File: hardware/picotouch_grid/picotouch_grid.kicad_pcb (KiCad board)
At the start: 2 copper layers, 180 x 110 mm, 125 parts, among them U1 Pico, U2 TS20, U3 TS20

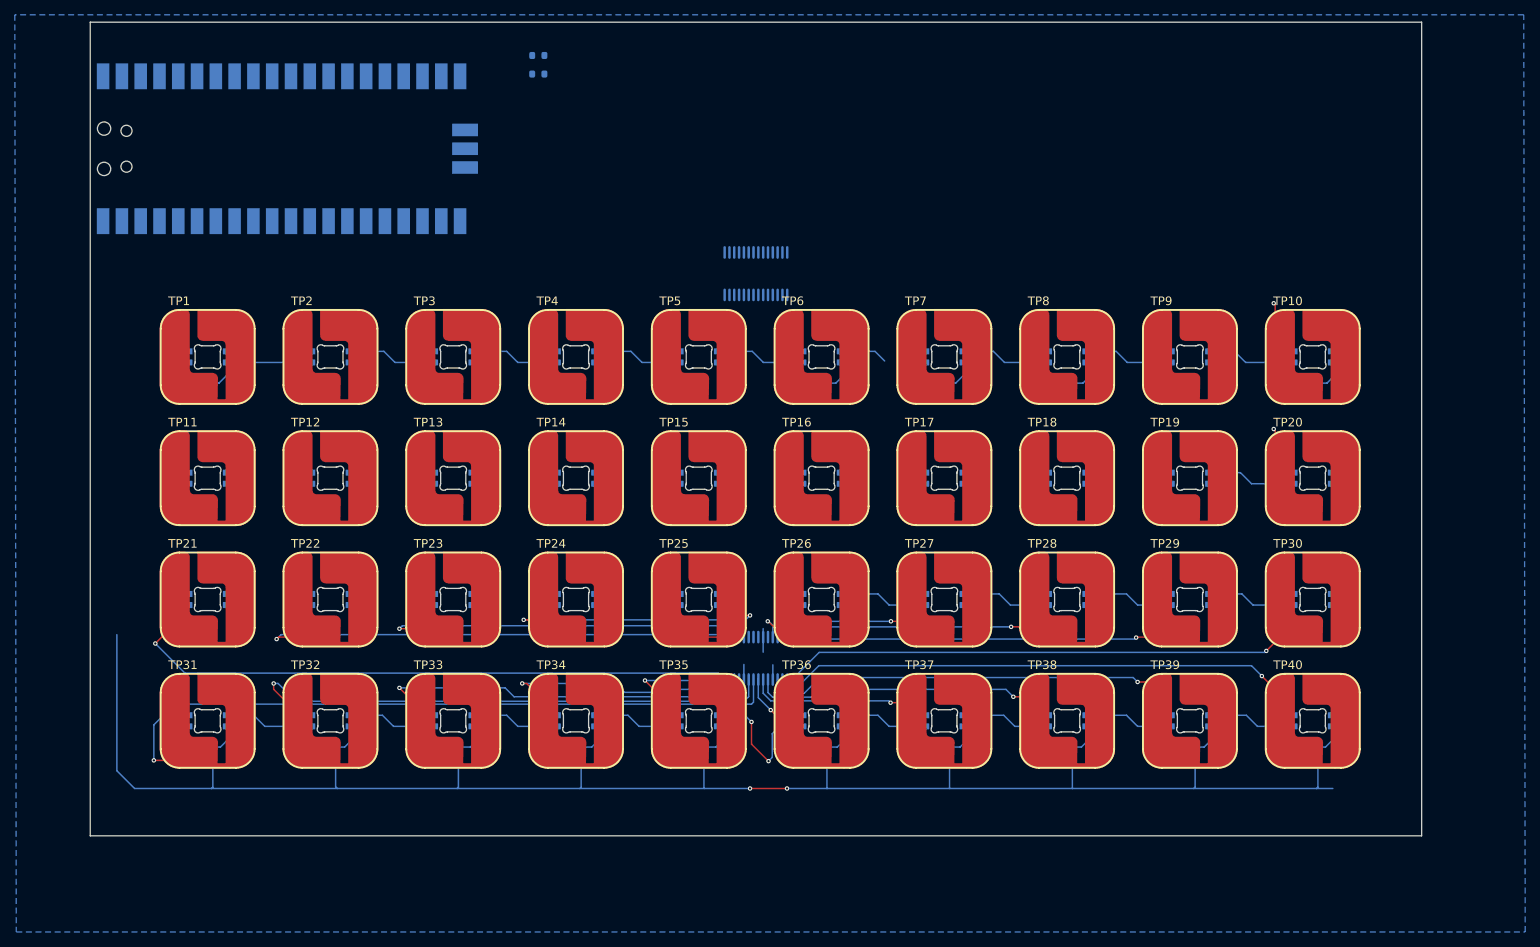
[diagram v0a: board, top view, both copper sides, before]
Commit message: more pcb routing done
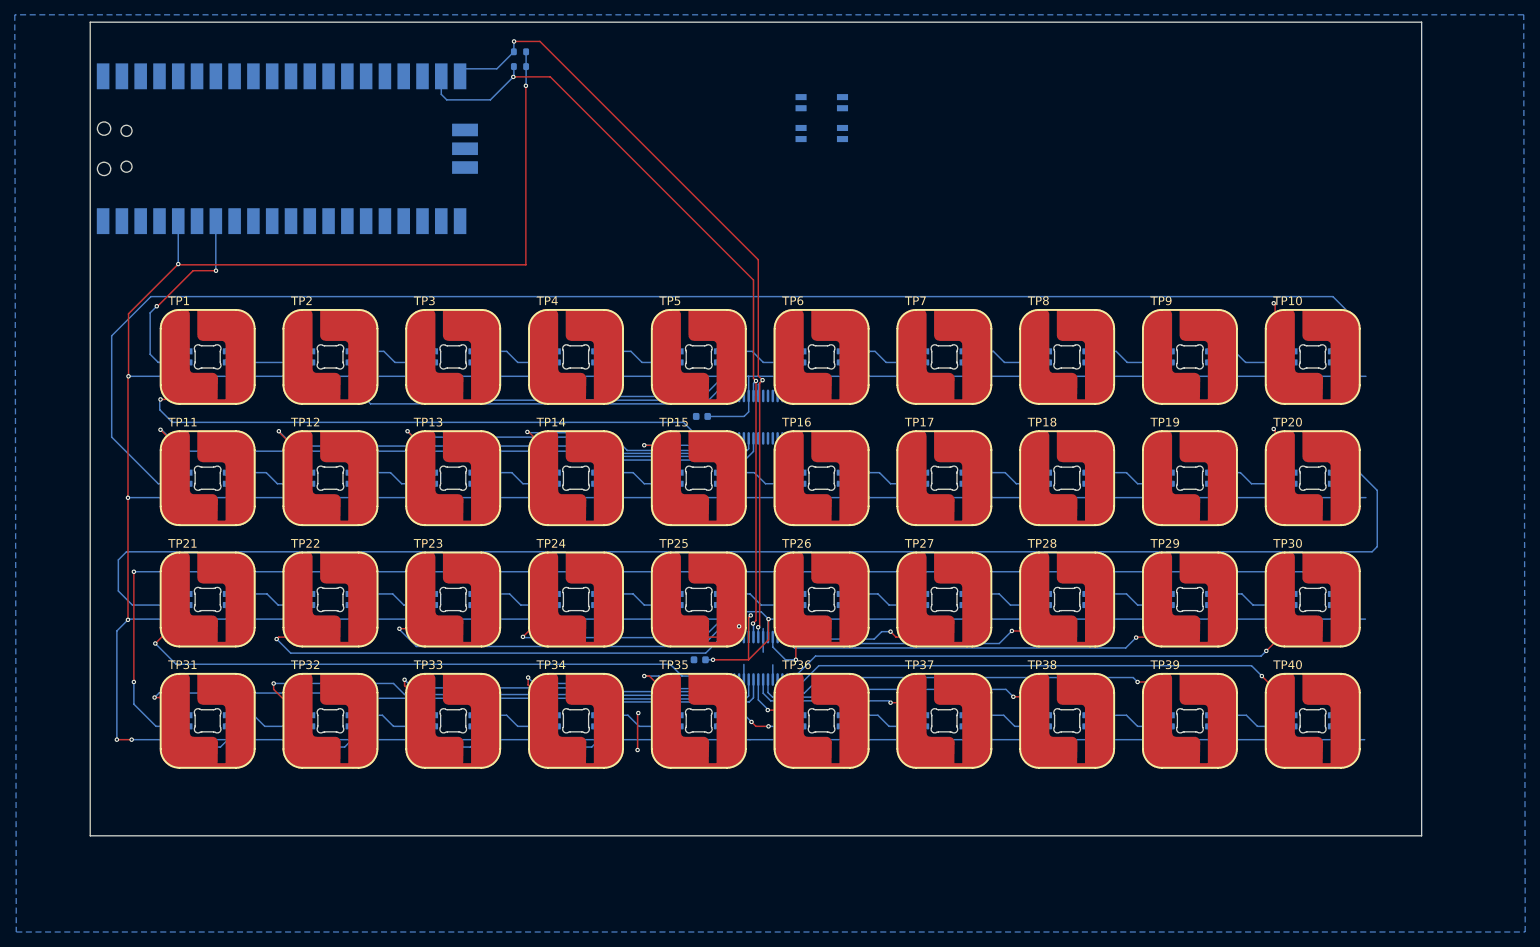
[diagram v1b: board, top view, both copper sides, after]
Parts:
- added C41: 1uF, Capacitor_SMD:C_0603_1608Metric, B.Cu at (119.7, 78.3)
- added C42: 1uF, Capacitor_SMD:C_0603_1608Metric, B.Cu at (119.4, 111.2)
- added U4: SK6812MINI-E_C5149201, easyeda2kicad:LED-SMD_L3.2-W2.8-TR, B.Cu at (135.9, 35.9)
- added U5: SK6812MINI-E_C5149201, easyeda2kicad:LED-SMD_L3.2-W2.8-TR, B.Cu at (135.9, 40.0)
- moved U2 19.4 mm to (127.0, 78.4)
- moved R2 3.90 mm to (95.1, 29.0)
- moved R1 2.89 mm to (95.1, 31.0)
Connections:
- LED1 pad 3: unconnected-(LED1-DIN-Pad3) -> /NEOPIXEL_DATA
- U1 pad 34: unconnected-(U1-GPIO28_ADC2-Pad34) -> /NEOPIXEL_DATA
- U2 pad 11: unconnected-(U2-CS13-Pad11) -> /tp13
- U2 pad 12: unconnected-(U2-CS14-Pad12) -> /tp14
- U2 pad 13: unconnected-(U2-CS15-Pad13) -> /tp15
- U2 pad 14: unconnected-(U2-CS16-Pad14) -> /tp1
- U2 pad 8: unconnected-(U2-CS11-Pad8) -> /tp11
- U2 pad 9: unconnected-(U2-CS12-Pad9) -> /tp12
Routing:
- net +3V3: track 305.9 -> 979.5 mm, vias 2 -> 10
- net Net-(LED10-DOUT): track 0.00 -> 204.5 mm
- net Net-(LED20-DOUT): track 0.00 -> 199.9 mm
- net Net-(LED30-DOUT): track 0.00 -> 191.1 mm, vias 0 -> 2
- net /TOUCH_SCL: track 0.00 -> 110.7 mm, vias 0 -> 3
- net /TOUCH_SDA: track 0.00 -> 108.9 mm, vias 0 -> 3
- net /tp11: track 0.00 -> 96.3 mm, vias 0 -> 1
- net /tp1: track 0.00 -> 81.0 mm, vias 0 -> 1
- net /tp12: track 0.00 -> 79.0 mm, vias 0 -> 1
- net /tp13: track 0.00 -> 59.6 mm, vias 0 -> 1
- net unconnected-(U2-CS17-Pad15): track 0.00 -> 49.4 mm
- net /tp14: track 0.00 -> 42.4 mm, vias 0 -> 1
- net unconnected-(U2-CS18-Pad16): track 0.00 -> 34.5 mm
- net /NEOPIXEL_DATA: track 0.00 -> 30.0 mm, vias 0 -> 2
- net /tp15: track 0.00 -> 24.0 mm, vias 0 -> 1
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
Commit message: pads mostly routed
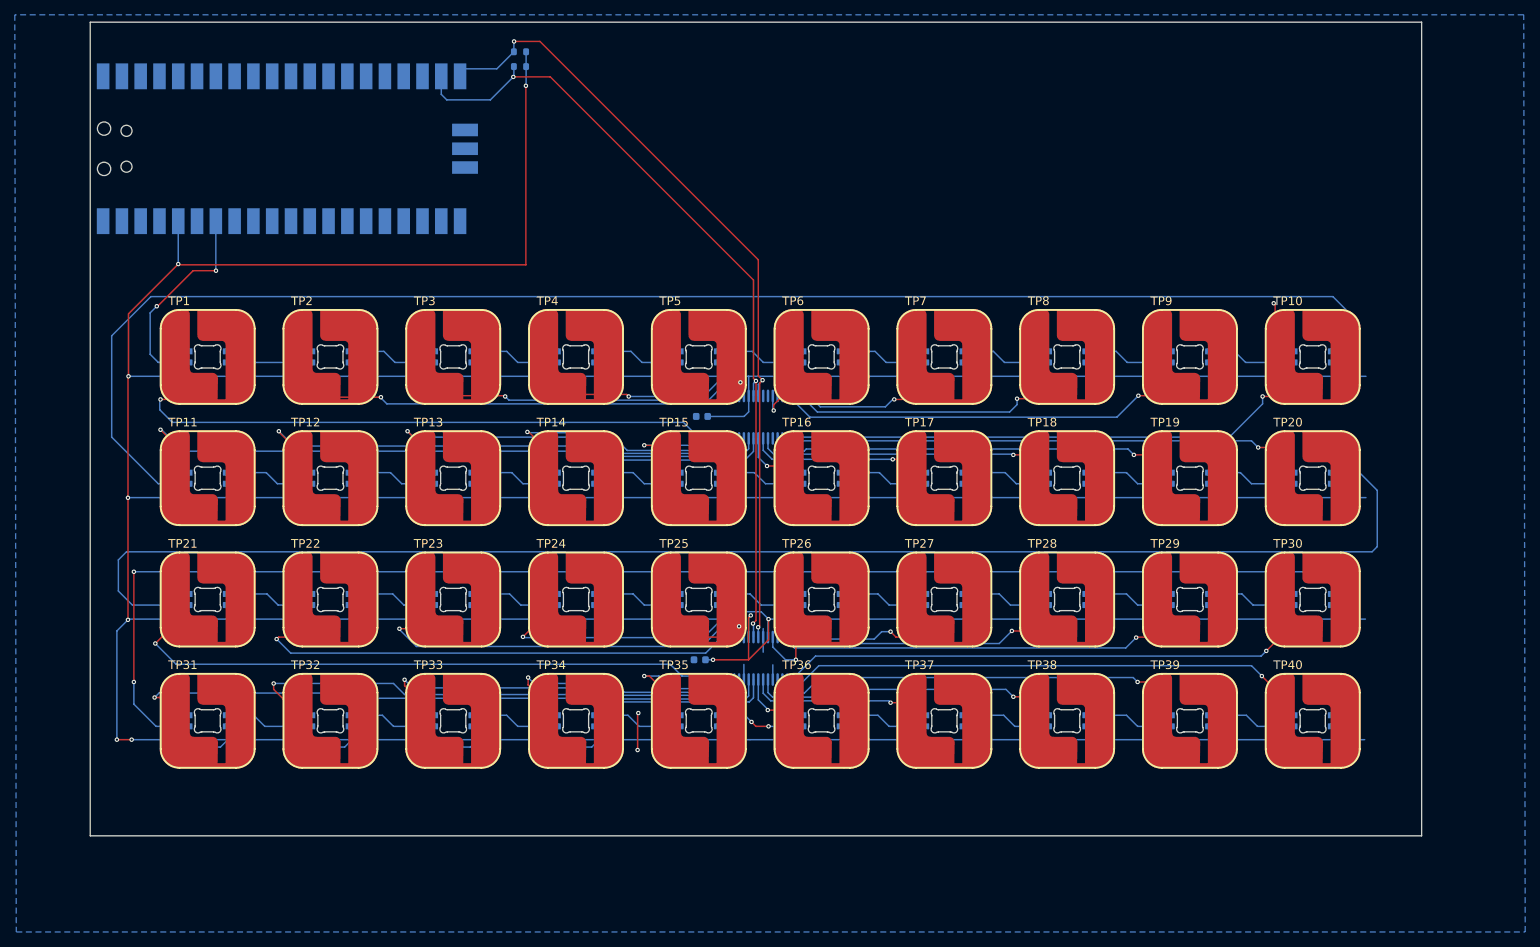
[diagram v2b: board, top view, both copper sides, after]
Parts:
- removed U4, U5: SK6812MINI-E_C5149201, easyeda2kicad:LED-SMD_L3.2-W2.8-TR
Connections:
- U1 pad 33: GND -> unconnected-(U1-AGND-Pad33)
- U2 pad 1: unconnected-(U2-CS5-Pad1) -> /tp10
- U2 pad 15: unconnected-(U2-CS17-Pad15) -> /tp2
- U2 pad 16: unconnected-(U2-CS18-Pad16) -> /tp3
- U2 pad 17: unconnected-(U2-CS19-Pad17) -> /tp4
- U2 pad 18: unconnected-(U2-CS20-Pad18) -> /tp5
- U2 pad 2: unconnected-(U2-CS6-Pad2) -> /tp20
- U2 pad 25: unconnected-(U2-CS1-Pad25) -> /tp6
- U2 pad 26: unconnected-(U2-CS2-Pad26) -> /tp7
- U2 pad 27: unconnected-(U2-CS3-Pad27) -> /tp8
- U2 pad 28: unconnected-(U2-CS4-Pad28) -> /tp9
- U2 pad 3: unconnected-(U2-CS7-Pad3) -> /tp19
- U2 pad 5: unconnected-(U2-CS8-Pad5) -> /tp18
- U2 pad 6: unconnected-(U2-CS9-Pad6) -> /tp17
- U2 pad 7: unconnected-(U2-CS10-Pad7) -> /tp16
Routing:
- net /tp10: track 12.4 -> 81.4 mm, vias 1 -> 2
- net /tp20: track 11.8 -> 77.5 mm
- net /tp2: track 0.00 -> 59.6 mm, vias 0 -> 1
- net /tp19: track 0.00 -> 52.4 mm, vias 0 -> 1
- net /tp9: track 0.00 -> 51.8 mm, vias 0 -> 1
- net unconnected-(U2-CS17-Pad15): track 49.4 -> 0.00 mm
- net /tp3: track 0.00 -> 44.8 mm, vias 0 -> 1
- net /tp8: track 0.00 -> 37.7 mm, vias 0 -> 1
- net /tp18: track 0.00 -> 36.5 mm, vias 0 -> 1
- net unconnected-(U2-CS18-Pad16): track 34.5 -> 0.00 mm
- net /tp4: track 0.00 -> 29.0 mm, vias 0 -> 1
- net /tp7: track 0.00 -> 21.0 mm, vias 0 -> 1
- net /tp17: track 0.00 -> 20.9 mm, vias 0 -> 1
- net unconnected-(U2-CS19-Pad17): track 19.6 -> 0.00 mm
- net /tp16: track 0.00 -> 6.27 mm, vias 0 -> 1
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
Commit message: pcb captouch routing passes DRC
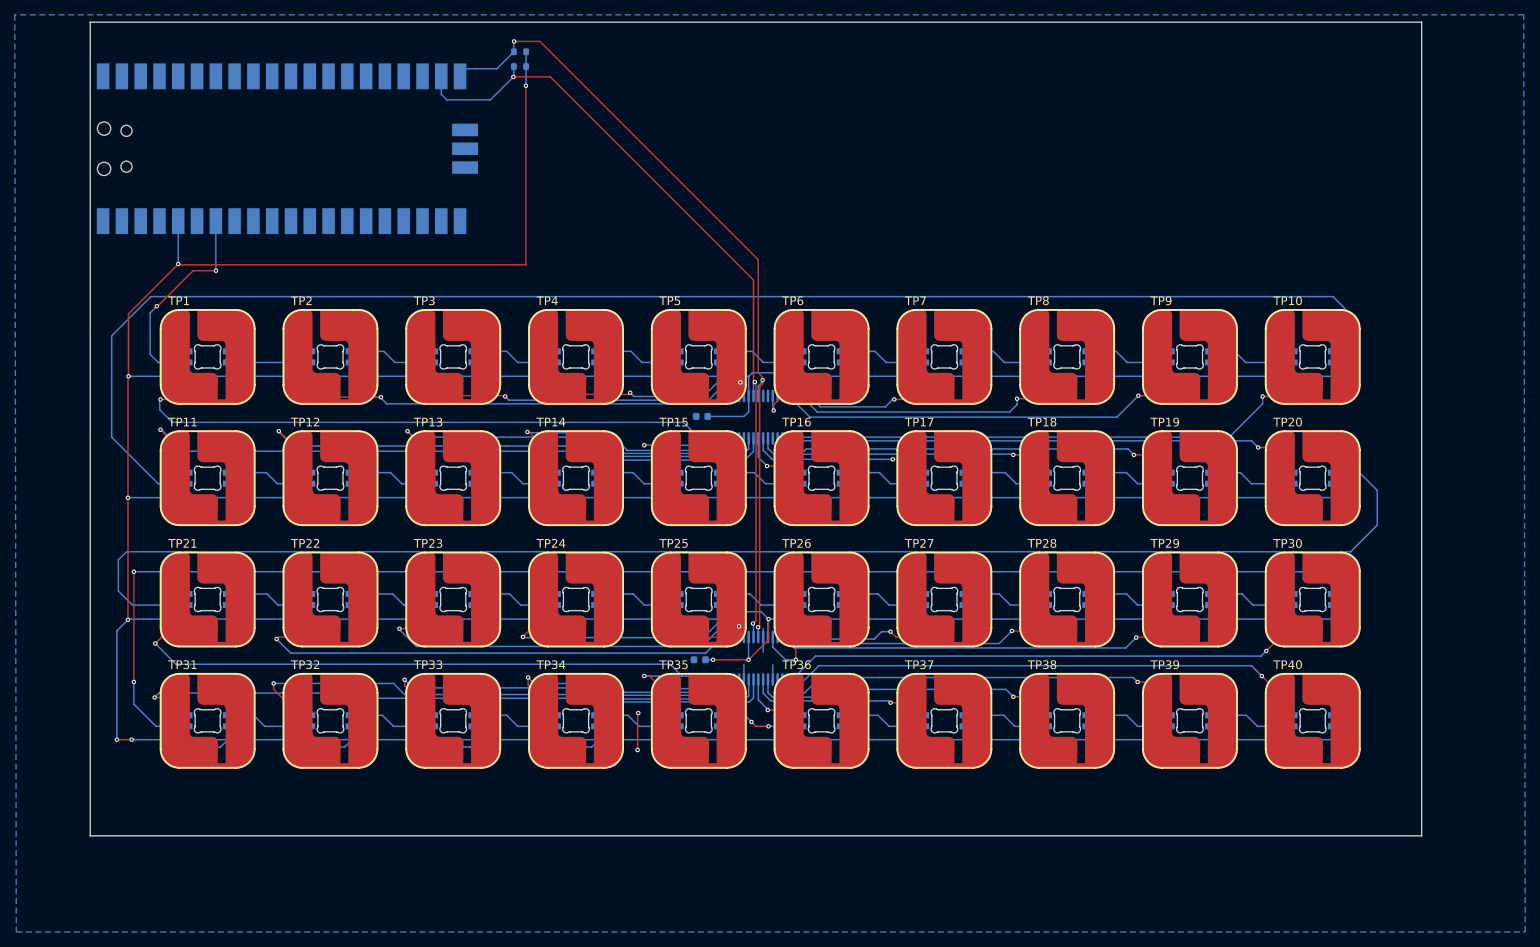
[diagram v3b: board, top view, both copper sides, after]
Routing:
- net +3V3: track 979.5 -> 953.7 mm
- net /tp10: track 81.4 -> 69.0 mm, vias 2 -> 1
- net Net-(LED20-DOUT): track 199.9 -> 198.2 mm
